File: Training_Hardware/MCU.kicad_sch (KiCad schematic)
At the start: 2 parts, among them J1 RJ45_LED_Shielded, U1 Teensy4.1_DEV-16771

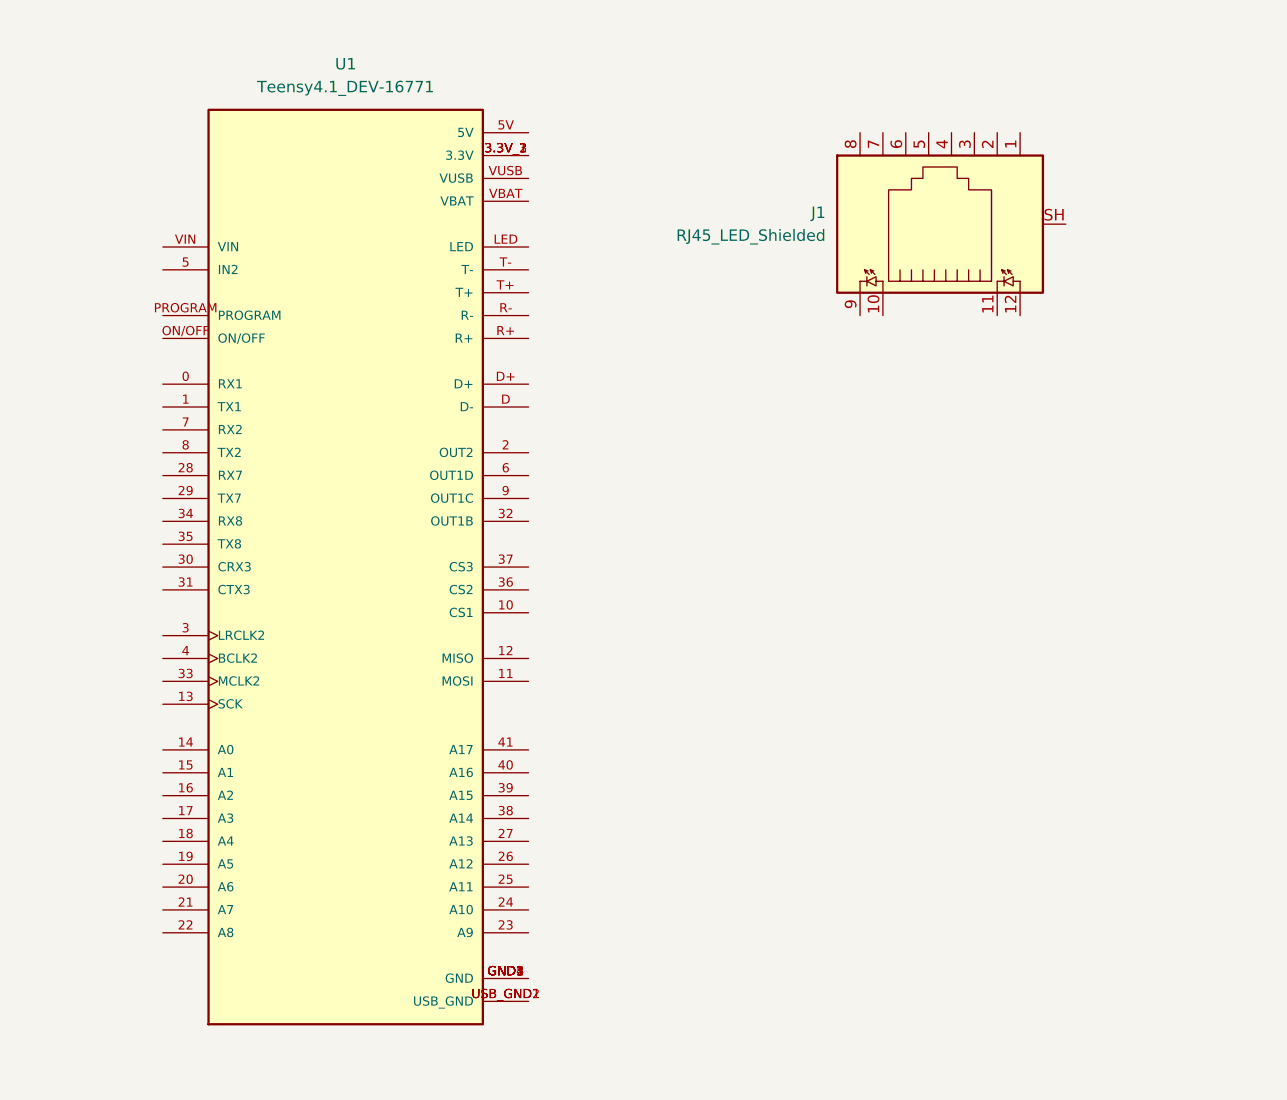
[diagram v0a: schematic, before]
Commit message: add ethernet
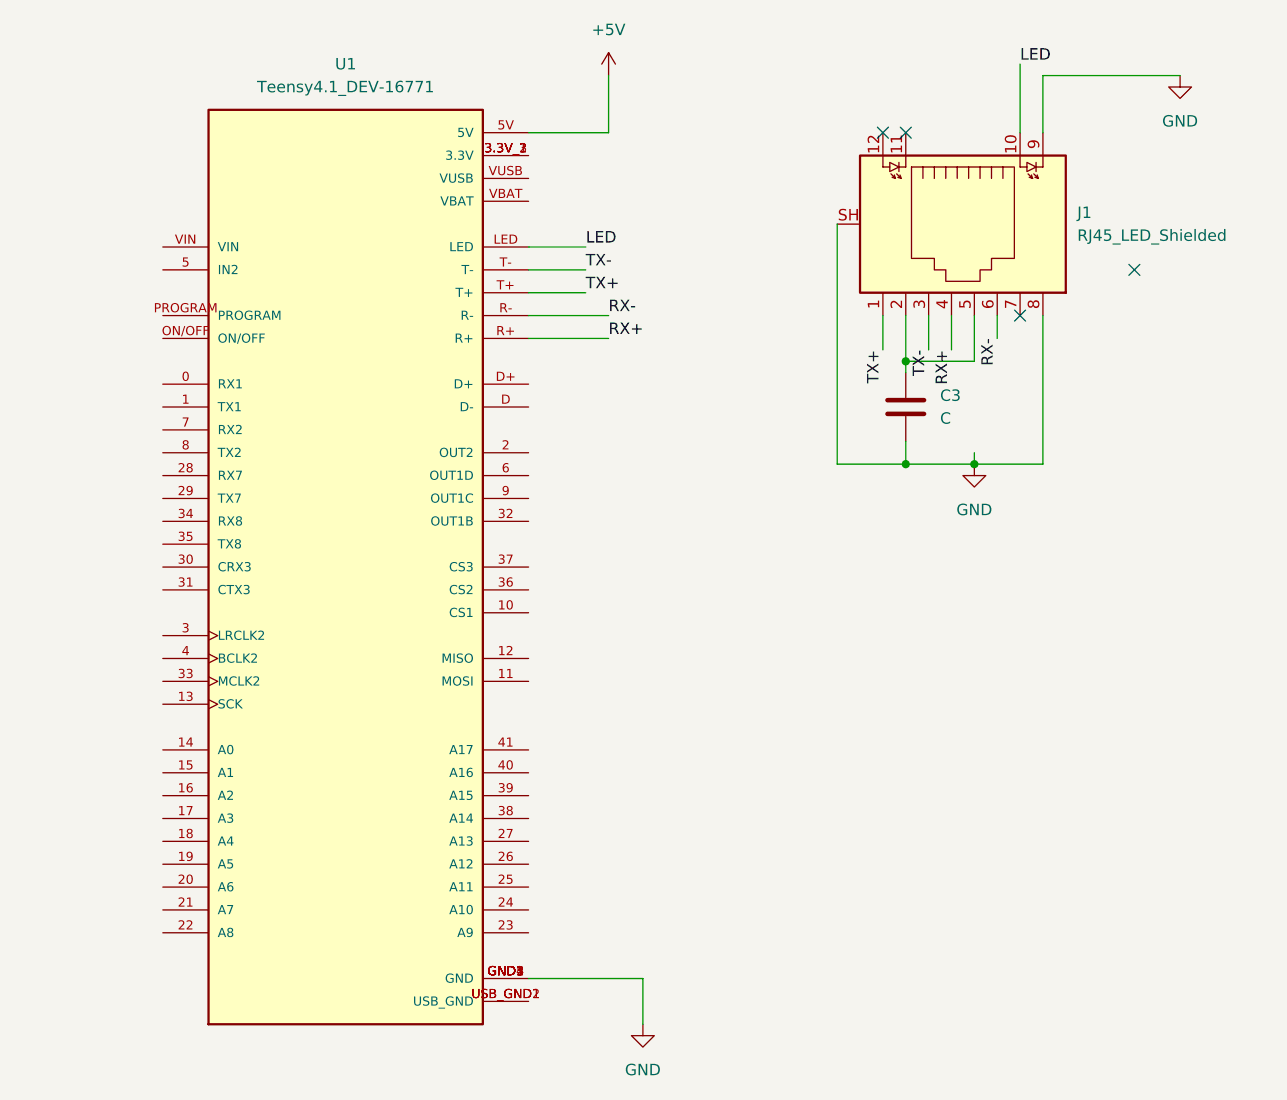
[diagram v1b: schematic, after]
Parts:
- added C3: C, symbol Device:C
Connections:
- net +5V: now reaches U1.5V
- net GND: now reaches U1.GND1 (GND), U1.GND2 (GND), U1.GND3 (GND), U1.GND4 (GND), U1.GND5 (GND)
- net GND: now also J1.8, J1.9, J1.SH, C3.2
- net LED: now reaches U1.LED
- net LED: now also J1.10
- net RX+: now reaches U1.R+
- net RX+: now also J1.4
- net RX-: now reaches U1.R-
- net RX-: now also J1.6
- net TX+: now reaches U1.T+
- net TX+: now also J1.1
- net TX-: now reaches U1.T-
- net TX-: now also J1.3
- net at J1.2: now also J1.5, C3.1
- no-connect marks 0 -> 4
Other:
- moved on the sheet: J1

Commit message: Finish Schematic
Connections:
- net STBY: now reaches U1.2 (OUT2)
- net CTX1: now reaches U1.22 (A8)
- net CRX1: now reaches U1.23 (A9)
- net +3V3: now reaches U1.3.3V_1 (3.3V), U1.3.3V_2 (3.3V), U1.3.3V_3 (3.3V)
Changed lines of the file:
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@@
+	(wire
+		(pts
+			(xy 88.9 132.08) (xy 104.14 132.08)
+		)
+		(stroke
+			(width 0)
+			(type default)
+		)
+	)
 	(wire
 		(pts
@@
 	(wire
 		(pts
+			(xy 88.9 45.72) (xy 101.6 45.72)
+		)
+		(stroke
+			(width 0)
+			(type default)
+		)
+	)
+	(wire
+		(pts
 			(xy 88.9 43.18) (xy 97.79 43.18)
 		)
@@
 	(wire
 		(pts
+			(xy 88.9 78.74) (xy 96.52 78.74)
+		)
+		(stroke
+			(width 0)
+			(type default)
+		)
+	)
+	(wire
+		(pts
 			(xy 140.97 63.5) (xy 140.97 66.04)
 		)
@@
 		(pts
 			(xy 146.05 43.18) (xy 146.05 36.83)
+		)
+		(stroke
+			(width 0)
+			(type default)
+		)
+	)
+	(wire
+		(pts
+			(xy 39.37 132.08) (xy 48.26 132.08)
 		)
 		(stroke
@@
 			)
 			(justify right bottom)
+		)
+	)
+	(hierarchical_label "STBY"
+		(shape output)
+		(at 96.52 78.74 0)
+		(effects
+			(font
+				(size 1.27 1.27)
+			)
+			(justify left)
+		)
+	)
+	(hierarchical_label "CTX1"
+		(shape output)
+		(at 39.37 132.08 180)
+		(effects
+			(font
+				(size 1.27 1.27)
+			)
+			(justify right)
+		)
+	)
+	(hierarchical_label "CRX1"
+		(shape input)
+		(at 104.14 132.08 0)
+		(effects
+			(font
+				(size 1.27 1.27)
+			)
+			(justify left)
 		)
 	)
@@
 					(unit 1)
 				)
+			)
+		)
+	)
+	(symbol
+		(lib_id "power:+3V3")
+		(at 101.6 45.72 0)
+		(unit 1)
+		(exclude_from_sim no)
+		(in_bom yes)
+		(on_board yes)
+		(dnp no)
+		(fields_autoplaced yes)
+		(property "Reference" "#PWR016"
+			(at 101.6 49.53 0)
+			(effects
+				(font
+					(size 1.27 1.27)
+				)
+				(hide yes)
+			)
+		)
+		(property "Value" "+3V3"
+			(at 101.6 40.64 0)
+			(effects
+				(font
+					(size 1.27 1.27)
+				)
+			)
+		)
+		(property "Footprint" ""
+			(at 101.6 45.72 0)
+			(effects
+				(font
+					(size 1.27 1.27)
+				)
+				(hide yes)
+			)
+		)
+		(property "Datasheet" ""
+			(at 101.6 45.72 0)
+			(effects
+				(font
+					(size 1.27 1.27)
+				)
+				(hide yes)
+			)
+		)
+		(property "Description" "Power symbol creates a global label with name \"+3V3\""
+			(at 101.6 45.72 0)
+			(effects
+				(font
+					(size 1.27 1.27)
+				)
+				(hide yes)
+			)
+		)
+		(pin "1"
+		)
+		(instances
+			(project ""
+				(path "/11bb8091-1487-4100-afd2-5aa288c40d4f/bab747f3-bfff-4257-8440-bff62be5f0b7"
+					(reference "#PWR016")
+					(unit 1)
+				)
